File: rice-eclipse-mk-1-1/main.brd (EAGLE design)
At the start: 100 x 81 mm, 56 parts, among them U1 LM1084ISX-5.0/NOPB, U2 THS4531IDRD8-M, U3 THS4531IDRD8-M, U4 THS4531IDRD8-M, U5 THS4531IDRD8-M, X1 2540-5

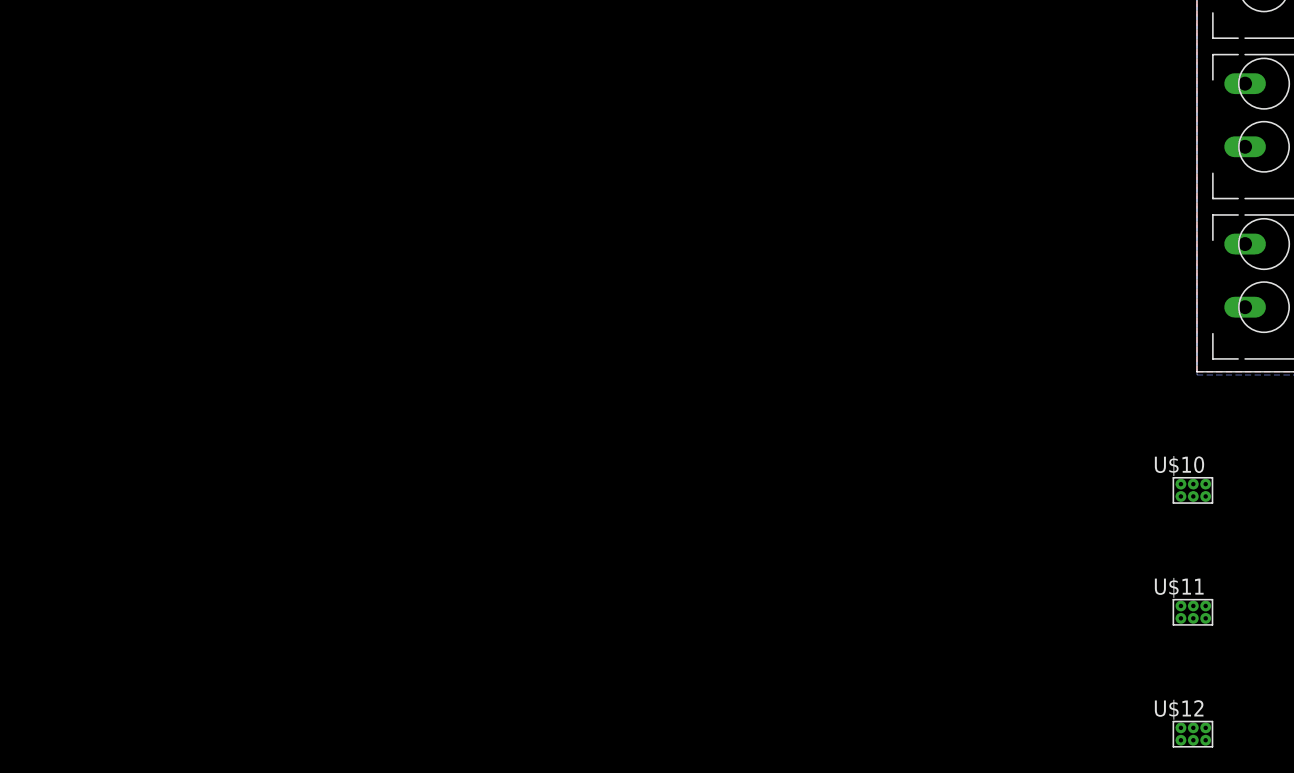
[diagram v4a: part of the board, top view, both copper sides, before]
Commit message: Added new libraries and fixed board annotation.
LEDS had to be removed in the process. Will re-add in next
version. I'm mostly just happy that the board is fixed.
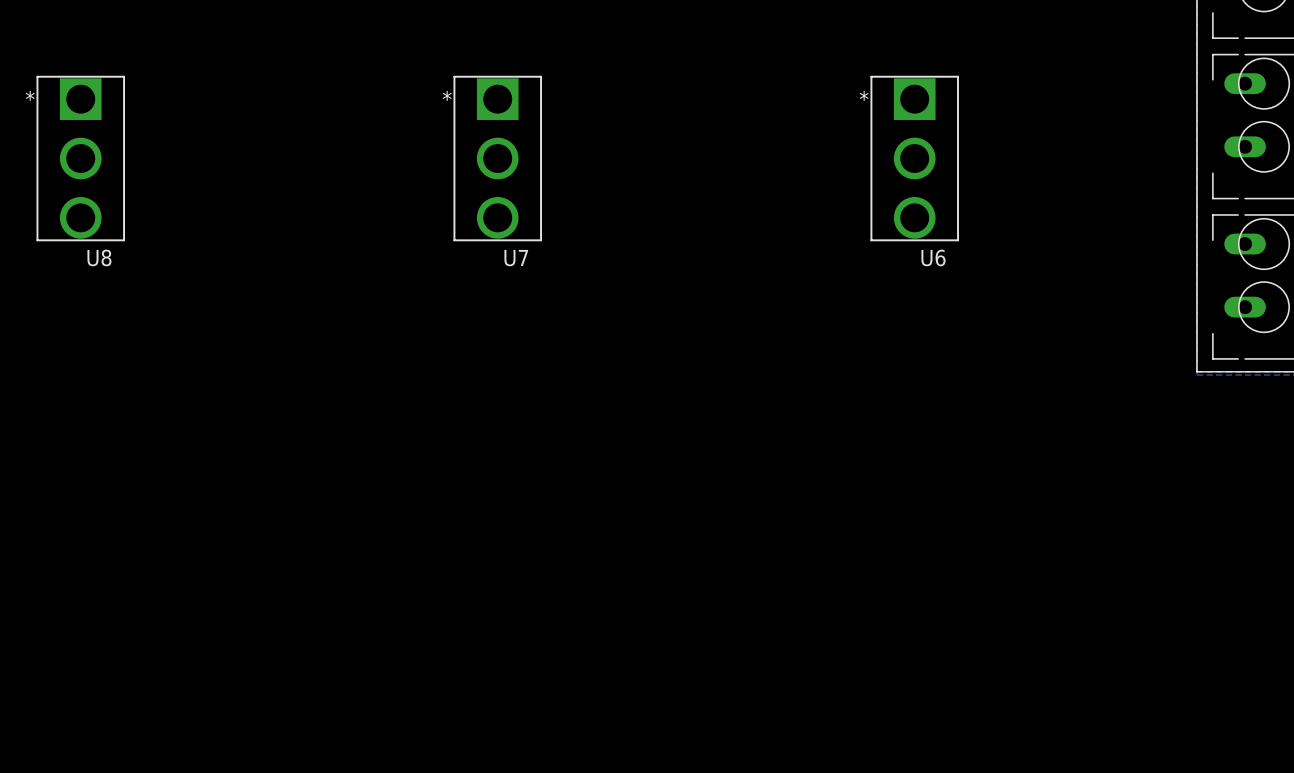
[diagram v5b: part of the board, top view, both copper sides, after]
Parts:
- removed U$10, U$11, U$12: SLIDE_SW, SLIDE_SW:SLIDE_SW
- added U6, U7, U8: 1101M2S3CQE2, SLIDE_SW:1101M2S3CQE2
- C10, C11, C12, C13, C3: device resistor:C0603 -> rcl:C0603
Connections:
- removed net DEBUG_3V3: U$11.P$1
- removed net DEBUG_5V: U$12.P$3
- new net +12V_DEBUG: U$1.A1, U$1.B1, U6.2
- new net +3V3_DEBUG: C4.1, REG1.2, U8.2
- new net +5V_DEBUG: C7.1, U1.2, U1.4, U7.2
- net +12V: now also U6.1; no longer U$1.A1, U$1.B1, U$10.P$2, U$10.P$3
- net +3V3: no longer C4.1, REG1.2, U$11.P$3
- net +5V: no longer C7.1, U$12.P$2, U1.2, U1.4

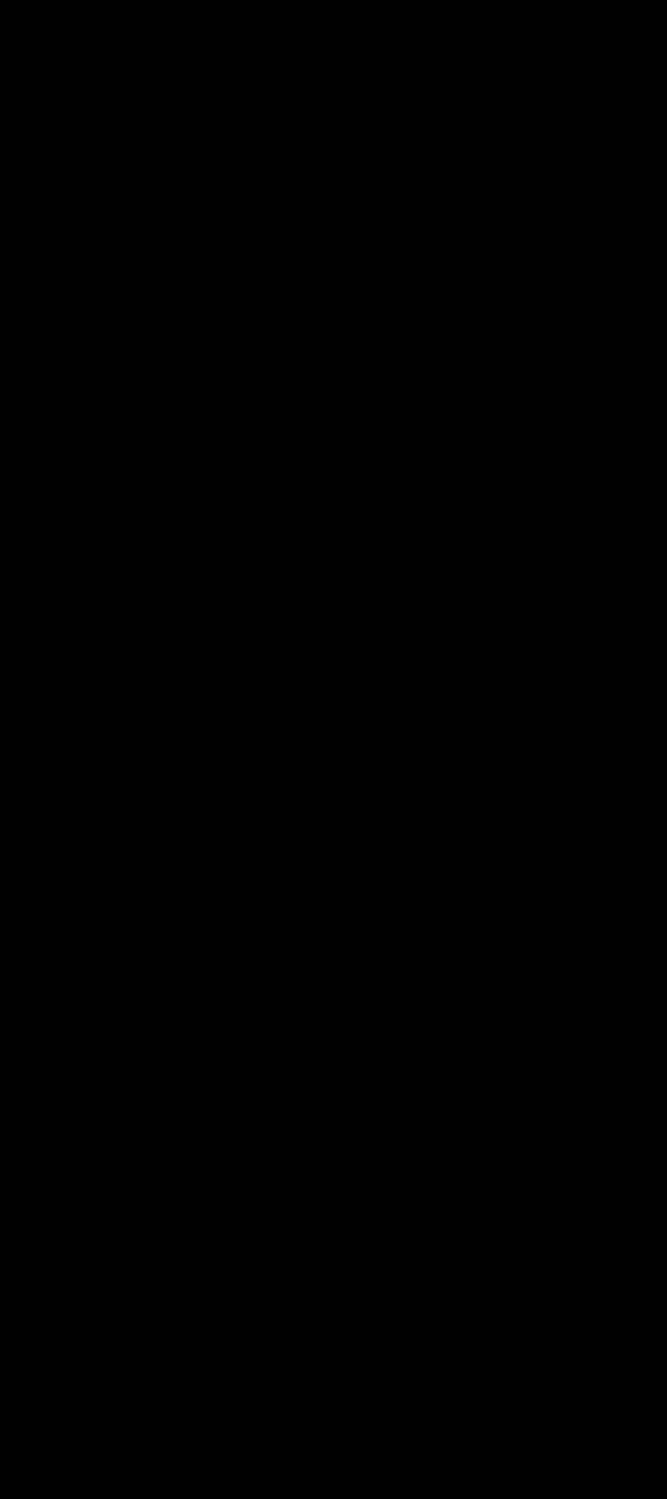
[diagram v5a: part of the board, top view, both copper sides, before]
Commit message: Added to the LEDs
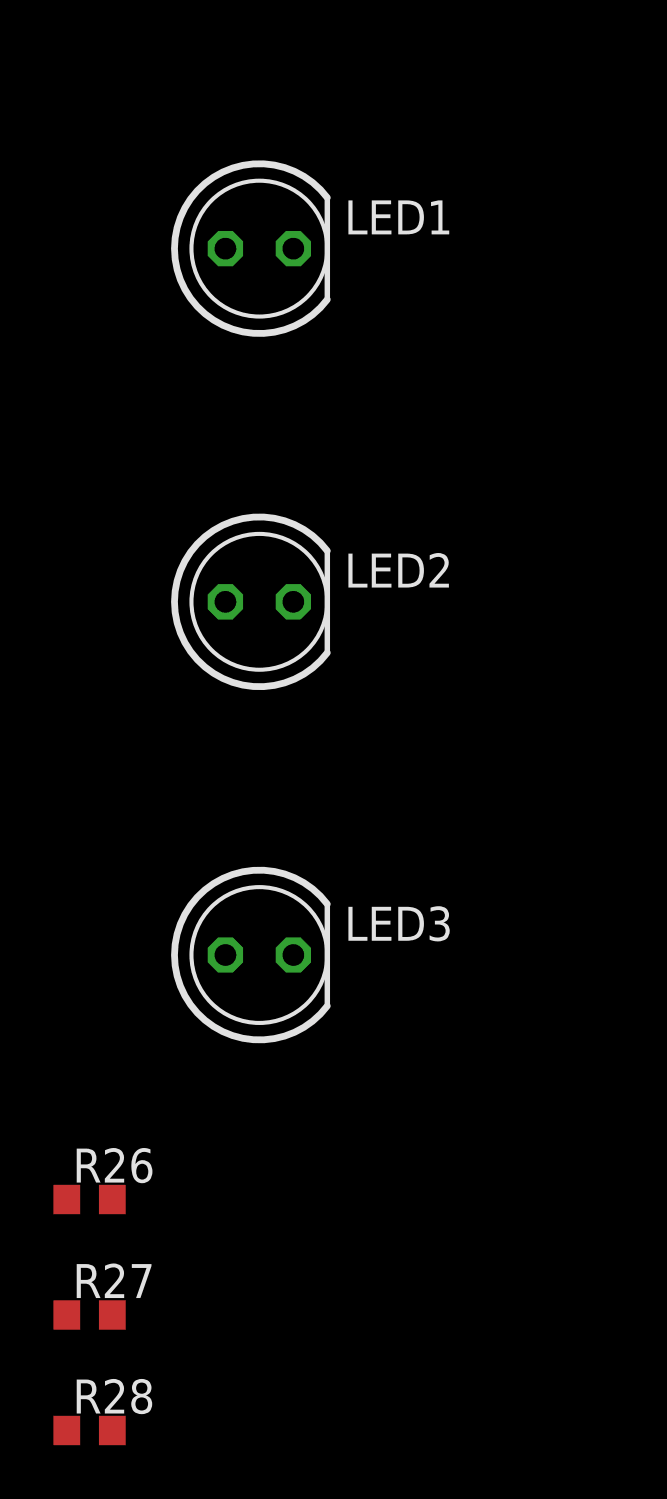
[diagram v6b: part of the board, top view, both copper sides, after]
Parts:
- added LED1, LED2, LED3: (no value), led:LED5MM
- added R26: 470, resistor:R0603
- added R27: 130, resistor:R0603
- added R28: 39, resistor:R0603
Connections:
- new net N$1: LED1.K, R26.2
- new net N$2: LED2.K, R27.1
- new net N$3: LED3.K, R28.1
- net +12V: now also LED1.A
- net +3V3: now also LED3.A
- net +5V: now also LED2.A
- net GND: now also R26.1, R27.2, R28.2

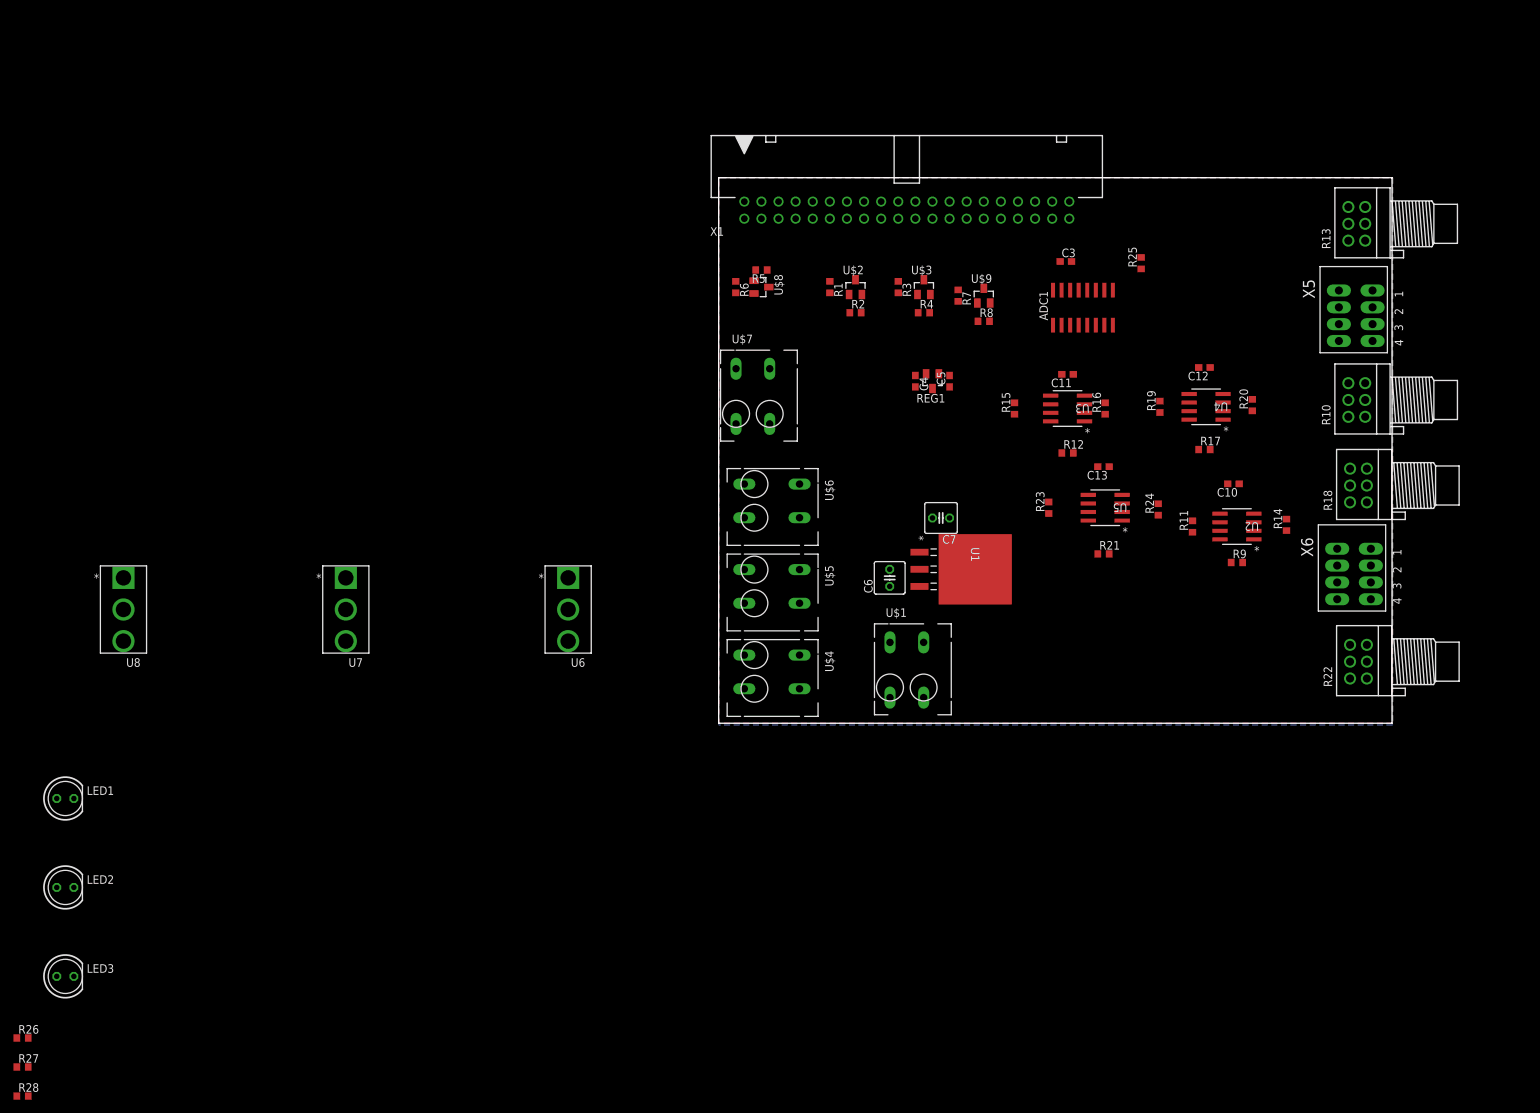
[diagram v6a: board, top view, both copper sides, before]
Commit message: Cleaned up the board, added adcs, debug pins.
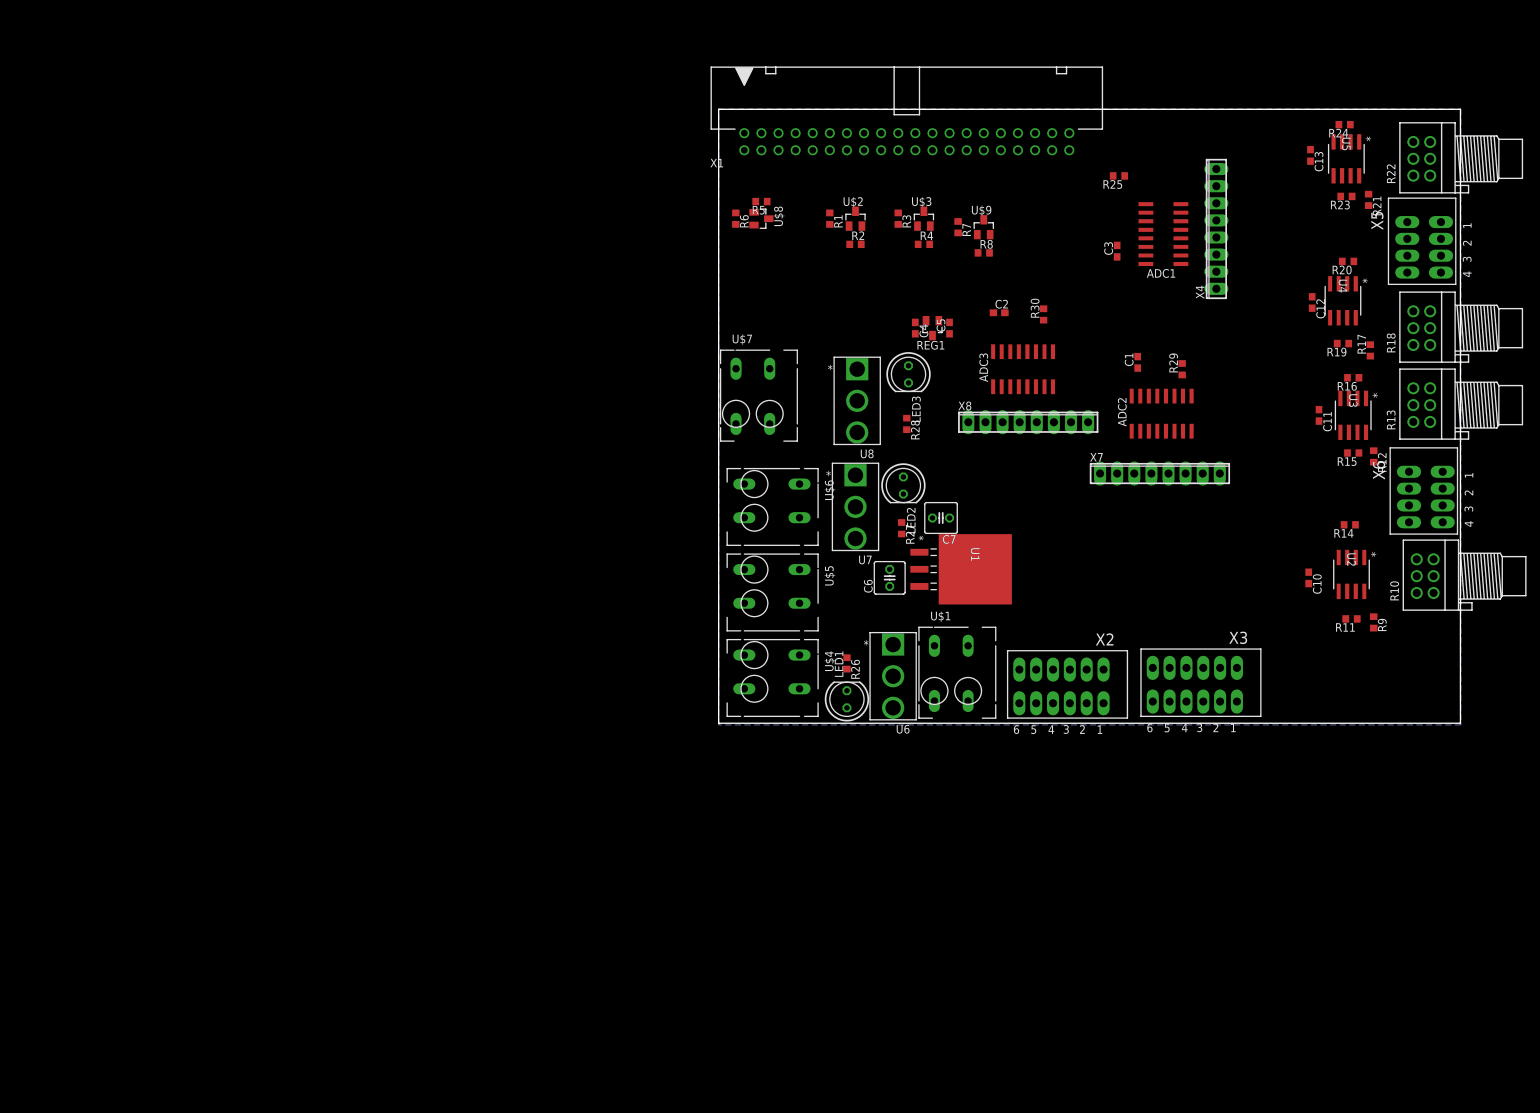
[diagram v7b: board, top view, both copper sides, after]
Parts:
- added ADC2, ADC3: MCP3208SN, microchip-extra:SO-16
- added C1, C2: 1UF, rcl:C0603
- added R29, R30: 500K, rcl:R0603
- added X2, X3: (no value), con-phoenix-250-extra:1770924
- added X4, X7, X8: (no value), con-phoenix-254:8POL254
- moved R28 165.0 mm to (27.9, 44.5), turned to 270 degrees
- moved LED3 153.9 mm to (28.2, 51.8), turned to 270 degrees
- moved R27 153.1 mm to (27.2, 29.0), turned to 270 degrees
- moved LED2 138.0 mm to (27.4, 35.3), turned to 270 degrees
- moved R26 134.5 mm to (19.1, 8.89), turned to 270 degrees
- moved LED1 117.0 mm to (19.1, 3.56), turned to 90 degrees
- moved U8 113.3 mm to (20.6, 43.2)
- moved U7 77.2 mm to (20.3, 27.4)
- moved R22 75.3 mm to (105.7, 83.8)
- moved R21 65.7 mm to (96.5, 77.7), turned to 270 degrees
- moved R23 64.0 mm to (93.2, 78.2), turned to 180 degrees
- moved R24 63.5 mm to (93.0, 88.9), turned to 180 degrees
- moved U5 63.0 mm to (93.2, 83.8), turned to 270 degrees
- moved C13 55.5 mm to (87.9, 84.3), turned to 270 degrees
- moved R15 50.7 mm to (94.2, 40.1), turned to 180 degrees
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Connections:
- new net ADC2_A0: ADC2.1, X7.1
- new net ADC2_A1: ADC2.2, X7.2
- new net ADC2_A2: ADC2.3, X7.3
- new net ADC2_A3: ADC2.4, X7.4
- new net ADC2_A4: ADC2.5, X7.5
- new net ADC2_A5: ADC2.6, X7.6
- new net ADC2_A6: ADC2.7, X7.7
- new net ADC2_A7: ADC2.8, X7.8
- new net ADC3_A0: ADC3.1, X8.1
- new net ADC3_A1: ADC3.2, X8.2
- new net ADC3_A2: ADC3.3, X8.3
- new net ADC3_A3: ADC3.4, X8.4
- new net ADC3_A4: ADC3.5, X8.5
- new net ADC3_A5: ADC3.6, X8.6
- new net ADC3_A6: ADC3.7, X8.7
- new net ADC3_A7: ADC3.8, X8.8
- net +3V3: now also ADC2.15, ADC2.16, ADC3.15, ADC3.16, C1.1, C2.1, R29.2, R30.2, U8.1
- net +5V: now also U7.1
- net ADC1_A0: now also R11.2, U2.5, X4.1; no longer R14.2, U2.4
- net ADC1_A1: now also R14.2, U2.4, X4.2; no longer R11.2, U2.5
- net ADC1_A2: now also R15.2, U3.5, X4.3; no longer R16.2, U3.4
- net ADC1_A3: now also R16.2, U3.4, X4.4; no longer R15.2, U3.5
- net ADC1_A4: now also R19.2, U4.5, X4.5; no longer R20.2, U4.4
- net ADC1_A5: now also R20.2, U4.4, X4.6; no longer R19.2, U4.5
- net ADC1_A6: now also R23.2, U5.5, X4.7; no longer R24.2, U5.4
- net ADC1_A7: now also R24.2, U5.4, X4.8; no longer R23.2, U5.5
- net ADC1_CS: now also ADC1.10
- net ADC2_CS: now also ADC2.10, R29.1
- net ADC3_CS: now also ADC3.10, R30.1
- net GND: now also ADC2.14, ADC2.9, ADC3.14, ADC3.9, C1.2, C2.2
- net LC_1_OUT+: now also X6.P$3, X6.P$7; no longer X5.P$1, X5.P$5
- net LC_1_OUT-: now also X6.P$4, X6.P$8; no longer X5.P$2, X5.P$6
- net LC_2_OUT+: now also X6.P$1, X6.P$5; no longer X5.P$3, X5.P$7
- net LC_2_OUT-: now also X6.P$2, X6.P$6; no longer X5.P$4, X5.P$8
- net LC_3_OUT+: now also X5.P$3, X5.P$7; no longer X6.P$1, X6.P$5
- net LC_3_OUT-: now also X5.P$4, X5.P$8; no longer X6.P$2, X6.P$6
- net LC_4_OUT+: now also X5.P$1, X5.P$5; no longer X6.P$3, X6.P$7
- net LC_4_OUT-: now also X5.P$2, X5.P$6; no longer X6.P$4, X6.P$8
- net MISO: now also ADC1.12, ADC2.12, ADC3.12
- net MOSI: now also ADC1.11, ADC2.11, ADC3.11
- net SCLK: now also ADC1.13, ADC2.13, ADC3.13
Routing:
- removed copper zone on layer 1, net GND
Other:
- board size 100 x 81 mm -> 110.2 x 91.2 mm

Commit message: Added more board parts.
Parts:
- removed U7, U8: 1101M2S3CQE2, SLIDE_SW:1101M2S3CQE2
- added IC1, IC2, IC3, IC4: LMV321LICTRT, st-microelectronics-extra:SOT23-5
- moved LED3 6.60 mm to (21.6, 51.8)
- moved R28 6.36 mm to (21.6, 44.2)
- moved LED2 5.59 mm to (21.8, 35.3)
- moved R27 5.33 mm to (21.8, 29.0)
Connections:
- removed net +3V3_DEBUG: C4.1, REG1.2, U8.2
- removed net +5V_DEBUG: C7.1, U1.2, U1.4, U7.2
- net +3V3: now also C4.1, REG1.2; no longer U8.1
- net +5V: now also C7.1, U1.2, U1.4; no longer U7.1
- net ADC2_A0: now also X2.P$12, X2.P$6
- net ADC2_A1: now also X2.P$11, X2.P$5
- net ADC2_A2: now also X2.P$10, X2.P$4
- net ADC2_A3: now also X2.P$3, X2.P$9
